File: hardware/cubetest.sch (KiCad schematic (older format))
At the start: 21 parts, among them J1 In, J10 GS2, J11 GS2, J2 Out, J3 pwr1, J4 pwr2, J5 USB_OTG, J6 GS3, J7 GS3, J8 GS3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

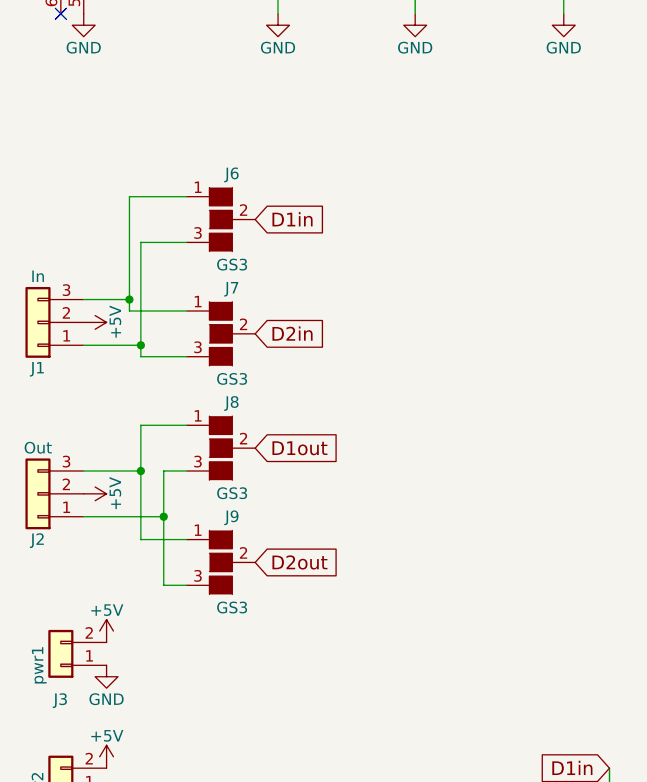
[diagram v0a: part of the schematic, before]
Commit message: remove solder bridges
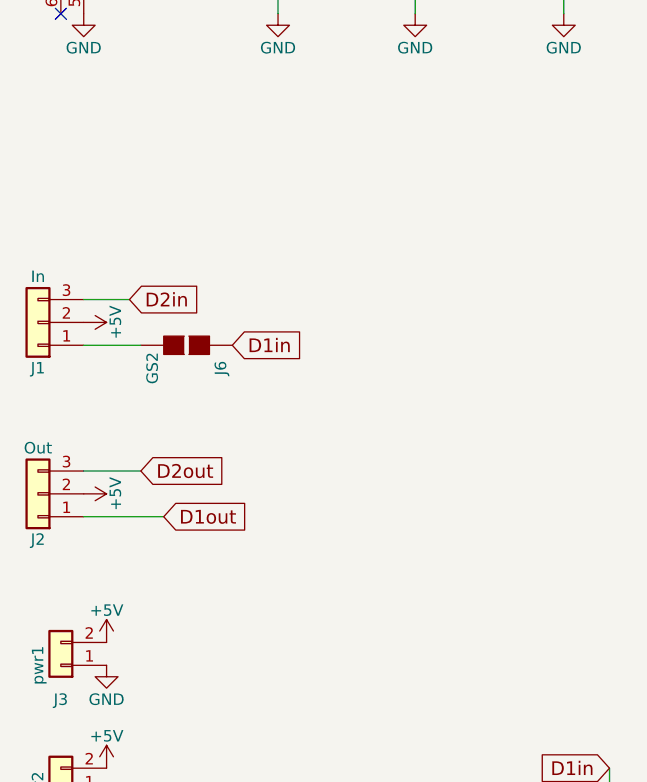
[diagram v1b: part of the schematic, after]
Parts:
- removed J6, J7, J8, J9: GS3, Connect:GS3, symbol GS3
- added J6: GS2, Connect:GS2, symbol GS2
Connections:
- net D1in: now also J6.1 (G1)
- net D1out: now also J2.1 (Pin_1)
- net D2in: now also J1.3 (Pin_3)
- net D2out: now also J2.3 (Pin_3)
- net at J1.1 (Pin_1): now also J6.2 (G2)
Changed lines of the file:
@@
 NoConn ~ 1900 1500
 NoConn ~ 1500 1700
-Text GLabel 2350 2600 2    60   Input ~ 0
+Text GLabel 2250 3150 2    60   Input ~ 0
 D1in
 $Comp
@@
 Text GLabel 7350 4050 2    60   Input ~ 0
 D1in
-Text GLabel 2350 3600 2    60   Input ~ 0
+Text GLabel 1950 3900 2    60   Input ~ 0
 D1out
 $Comp
@@
 Wire Wire Line
 	1600 3150 1850 3150
-Connection ~ 1800 2950
-Connection ~ 1850 3150
 $Comp
 L ws2812b_wat U2
@@
 Wire Wire Line
 	3900 5000 3900 5150
-Text GLabel 2350 3100 2    60   Input ~ 0
+Text GLabel 1800 2950 2    60   Input ~ 0
 D2in
 Text GLabel 3850 5450 0    60   Input ~ 0
@@
 Wire Wire Line
 	3900 5450 3900 5350
-Text GLabel 2350 4100 2    60   Input ~ 0
+Text GLabel 1850 3700 2    60   Input ~ 0
 D2out
 Text GLabel 6500 5400 2    60   Input ~ 0
@@
 	-1   0    0    1
 $EndComp
-$Comp
-L GS3 J6
-U 1 1 59FAF174
-P 2200 2600
-F 0 "J6" H 2250 2800 50  0000 C CNN
-F 1 "GS3" H 2250 2401 50  0000 C CNN
-F 2 "Connect:GS3" V 2288 2526 50  0001 C CNN
-F 3 "" H 2200 2600 50  0001 C CNN
-	1    2200 2600
-	1    0    0    -1
-$EndComp
-$Comp
-L GS3 J7
-U 1 1 59FAF47D
-P 2200 3100
-F 0 "J7" H 2250 3300 50  0000 C CNN
-F 1 "GS3" H 2250 2901 50  0000 C CNN
-F 2 "Connect:GS3" V 2288 3026 50  0001 C CNN
-F 3 "" H 2200 3100 50  0001 C CNN
-	1    2200 3100
-	1    0    0    -1
-$EndComp
-Wire Wire Line
-	1800 2500 1800 3000
-Wire Wire Line
-	1800 2500 2050 2500
-Wire Wire Line
-	1850 2700 1850 3200
-Wire Wire Line
-	1850 2700 2050 2700
 Wire Wire Line
 	1600 2950 1800 2950
 Wire Wire Line
-	1800 3000 2050 3000
-Wire Wire Line
-	1850 3200 2050 3200
-$Comp
-L GS3 J8
-U 1 1 59FAFCFA
-P 2200 3600
-F 0 "J8" H 2250 3800 50  0000 C CNN
-F 1 "GS3" H 2250 3401 50  0000 C CNN
-F 2 "Connect:GS3" V 2288 3526 50  0001 C CNN
-F 3 "" H 2200 3600 50  0001 C CNN
-	1    2200 3600
-	1    0    0    -1
-$EndComp
-$Comp
-L GS3 J9
-U 1 1 59FAFD64
-P 2200 4100
-F 0 "J9" H 2250 4300 50  0000 C CNN
-F 1 "GS3" H 2250 3901 50  0000 C CNN
-F 2 "Connect:GS3" V 2288 4026 50  0001 C CNN
-F 3 "" H 2200 4100 50  0001 C CNN
-	1    2200 4100
-	1    0    0    -1
-$EndComp
-Wire Wire Line
 	1600 3700 1850 3700
 Wire Wire Line
-	1850 3500 1850 4000
-Wire Wire Line
-	1850 3500 2050 3500
-Wire Wire Line
-	1850 4000 2050 4000
-Connection ~ 1850 3700
-Wire Wire Line
 	1600 3900 1950 3900
-Wire Wire Line
-	1950 3700 1950 4200
-Wire Wire Line
-	1950 3700 2050 3700
-Wire Wire Line
-	1950 4200 2050 4200
-Connection ~ 1950 3900
 $Comp
 L GS2 J10
@@
 	0    1    1    0
 $EndComp
+$Comp
+L GS2 J6
+U 1 1 5A410B99
+P 2050 3150
+F 0 "J6" H 2150 3300 50  0000 C CNN
+F 1 "GS2" H 2150 3001 50  0000 C CNN
+F 2 "Connect:GS2" V 2124 3150 50  0001 C CNN
+F 3 "" H 2050 3150 50  0001 C CNN
+	1    2050 3150
+	0    1    1    0
+$EndComp

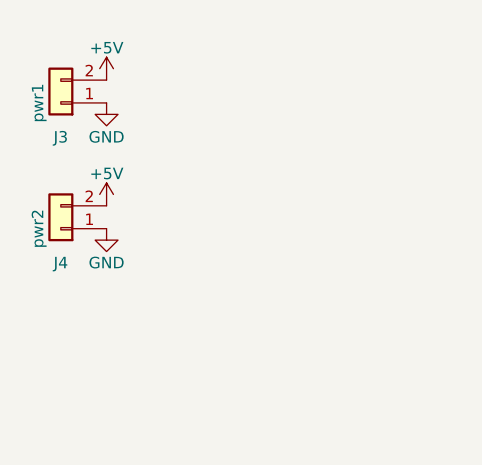
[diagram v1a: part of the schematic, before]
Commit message: fix pcb, added new pwr
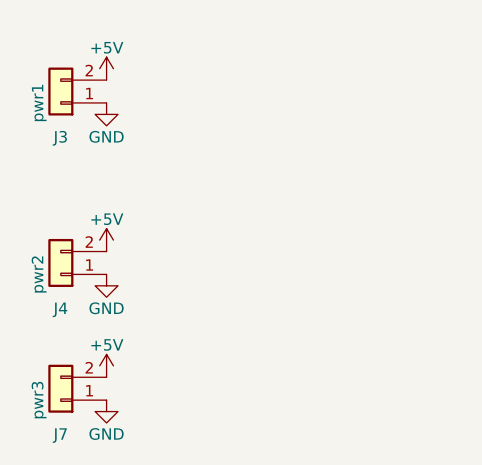
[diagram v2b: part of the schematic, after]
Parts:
- added J7: pwr3, Pin_Headers:Pin_Header_Straight_1x02_Pitch2.54mm, symbol Conn_01x02
- J10, J11, J6: footprint Connect:GS2 -> Connectors:GS2
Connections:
- net +5V: now also J7.2 (Pin_2)
- net GND: now also J7.1 (Pin_1)
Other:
- moved on the sheet: J4
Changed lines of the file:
@@
 L Conn_01x02 J4
 U 1 1 59F60FED
-P 1500 5100
-F 0 "J4" H 1500 5250 50  0000 C CNN
-F 1 "pwr2" V 1600 5100 50  0000 C CNN
-F 2 "Pin_Headers:Pin_Header_Straight_1x02_Pitch2.54mm" H 1500 5100 50  0001 C CNN
-F 3 "" H 1500 5100 50  0001 C CNN
-	1    1500 5100
+P 1500 5300
+F 0 "J4" H 1500 5450 50  0000 C CNN
+F 1 "pwr2" V 1600 5300 50  0000 C CNN
+F 2 "Pin_Headers:Pin_Header_Straight_1x02_Pitch2.54mm" H 1500 5300 50  0001 C CNN
+F 3 "" H 1500 5300 50  0001 C CNN
+	1    1500 5300
 	-1   0    0    1
 $EndComp
@@
 L +5V #PWR012
 U 1 1 59F87A18
-P 1700 5000
-F 0 "#PWR012" H 1700 4850 50  0001 C CNN
-F 1 "+5V" H 1700 5140 50  0000 C CNN
-F 2 "" H 1700 5000 50  0001 C CNN
-F 3 "" H 1700 5000 50  0001 C CNN
-	1    1700 5000
+P 1700 5200
+F 0 "#PWR012" H 1700 5050 50  0001 C CNN
+F 1 "+5V" H 1700 5340 50  0000 C CNN
+F 2 "" H 1700 5200 50  0001 C CNN
+F 3 "" H 1700 5200 50  0001 C CNN
+	1    1700 5200
 	1    0    0    -1
 $EndComp
@@
 L GND #PWR014
 U 1 1 59F87A7C
-P 1700 5100
-F 0 "#PWR014" H 1700 4850 50  0001 C CNN
-F 1 "GND" H 1700 4950 50  0000 C CNN
-F 2 "" H 1700 5100 50  0001 C CNN
-F 3 "" H 1700 5100 50  0001 C CNN
-	1    1700 5100
+P 1700 5300
+F 0 "#PWR014" H 1700 5050 50  0001 C CNN
+F 1 "GND" H 1700 5150 50  0000 C CNN
+F 2 "" H 1700 5300 50  0001 C CNN
+F 3 "" H 1700 5300 50  0001 C CNN
+	1    1700 5300
 	1    0    0    -1
 $EndComp
@@
 F 0 "J10" H 5250 5050 50  0000 C CNN
 F 1 "GS2" H 5250 4751 50  0000 C CNN
-F 2 "Connect:GS2" V 5224 4900 50  0001 C CNN
+F 2 "Connectors:GS2" V 5224 4900 50  0001 C CNN
 F 3 "" H 5150 4900 50  0001 C CNN
 	1    5150 4900
@@
 F 0 "J11" H 5250 5750 50  0000 C CNN
 F 1 "GS2" H 5250 5451 50  0000 C CNN
-F 2 "Connect:GS2" V 5224 5600 50  0001 C CNN
+F 2 "Connectors:GS2" V 5224 5600 50  0001 C CNN
 F 3 "" H 5150 5600 50  0001 C CNN
 	1    5150 5600
@@
 F 0 "J6" H 2150 3300 50  0000 C CNN
 F 1 "GS2" H 2150 3001 50  0000 C CNN
-F 2 "Connect:GS2" V 2124 3150 50  0001 C CNN
+F 2 "Connectors:GS2" V 2124 3150 50  0001 C CNN
 F 3 "" H 2050 3150 50  0001 C CNN
 	1    2050 3150
 	0    1    1    0
 $EndComp
+$Comp
+L Conn_01x02 J7
+U 1 1 5A422194
+P 1500 5850
+F 0 "J7" H 1500 6000 50  0000 C CNN
+F 1 "pwr3" V 1600 5850 50  0000 C CNN
+F 2 "Pin_Headers:Pin_Header_Straight_1x02_Pitch2.54mm" H 1500 5850 50  0001 C CNN
+F 3 "" H 1500 5850 50  0001 C CNN
+	1    1500 5850
+	-1   0    0    1
+$EndComp
+$Comp
+L GND #PWR023
+U 1 1 5A422204
+P 1700 5850
+F 0 "#PWR023" H 1700 5600 50  0001 C CNN
+F 1 "GND" H 1700 5700 50  0000 C CNN
+F 2 "" H 1700 5850 50  0001 C CNN
+F 3 "" H 1700 5850 50  0001 C CNN
+	1    1700 5850
+	1    0    0    -1
+$EndComp
+$Comp
+L +5V #PWR024
+U 1 1 5A422248
+P 1700 5750
+F 0 "#PWR024" H 1700 5600 50  0001 C CNN
+F 1 "+5V" H 1700 5890 50  0000 C CNN
+F 2 "" H 1700 5750 50  0001 C CNN
+F 3 "" H 1700 5750 50  0001 C CNN
+	1    1700 5750
+	1    0    0    -1
+$EndComp
 $EndSCHEMATC
